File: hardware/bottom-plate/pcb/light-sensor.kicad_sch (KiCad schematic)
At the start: 4 parts

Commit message: actually fixed it (merging moment)
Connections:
- net +5V renamed LED_5V

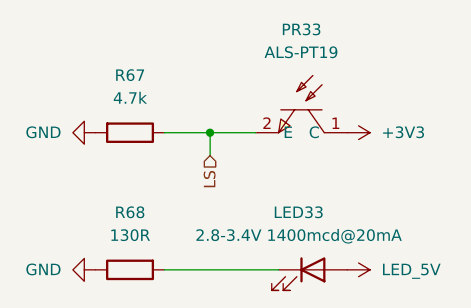
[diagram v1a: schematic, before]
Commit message: fixed bottom pcb alspt19 and leds
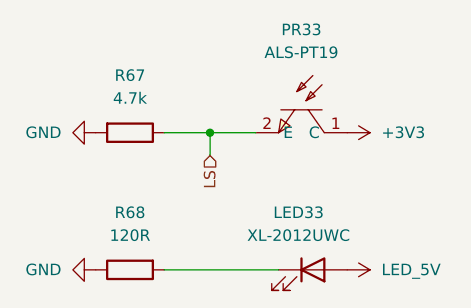
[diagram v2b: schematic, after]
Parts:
- LED33: value 2.8-3.4V 1400mcd@20mA -> XL-2012UWC
- R68: value 130R -> 120R
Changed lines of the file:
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@@
 			)
 		)
-		(property "Value" "2.8-3.4V 1400mcd@20mA"
+		(property "Value" "XL-2012UWC"
 			(at 178.7525 68.58 0)
 			(effects
@@
 			)
 		)
-		(property "Value" "130R"
+		(property "Value" "120R"
 			(at 160.02 68.58 90)
 			(effects
